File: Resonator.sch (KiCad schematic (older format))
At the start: 31 parts, among them U1 PCM3060

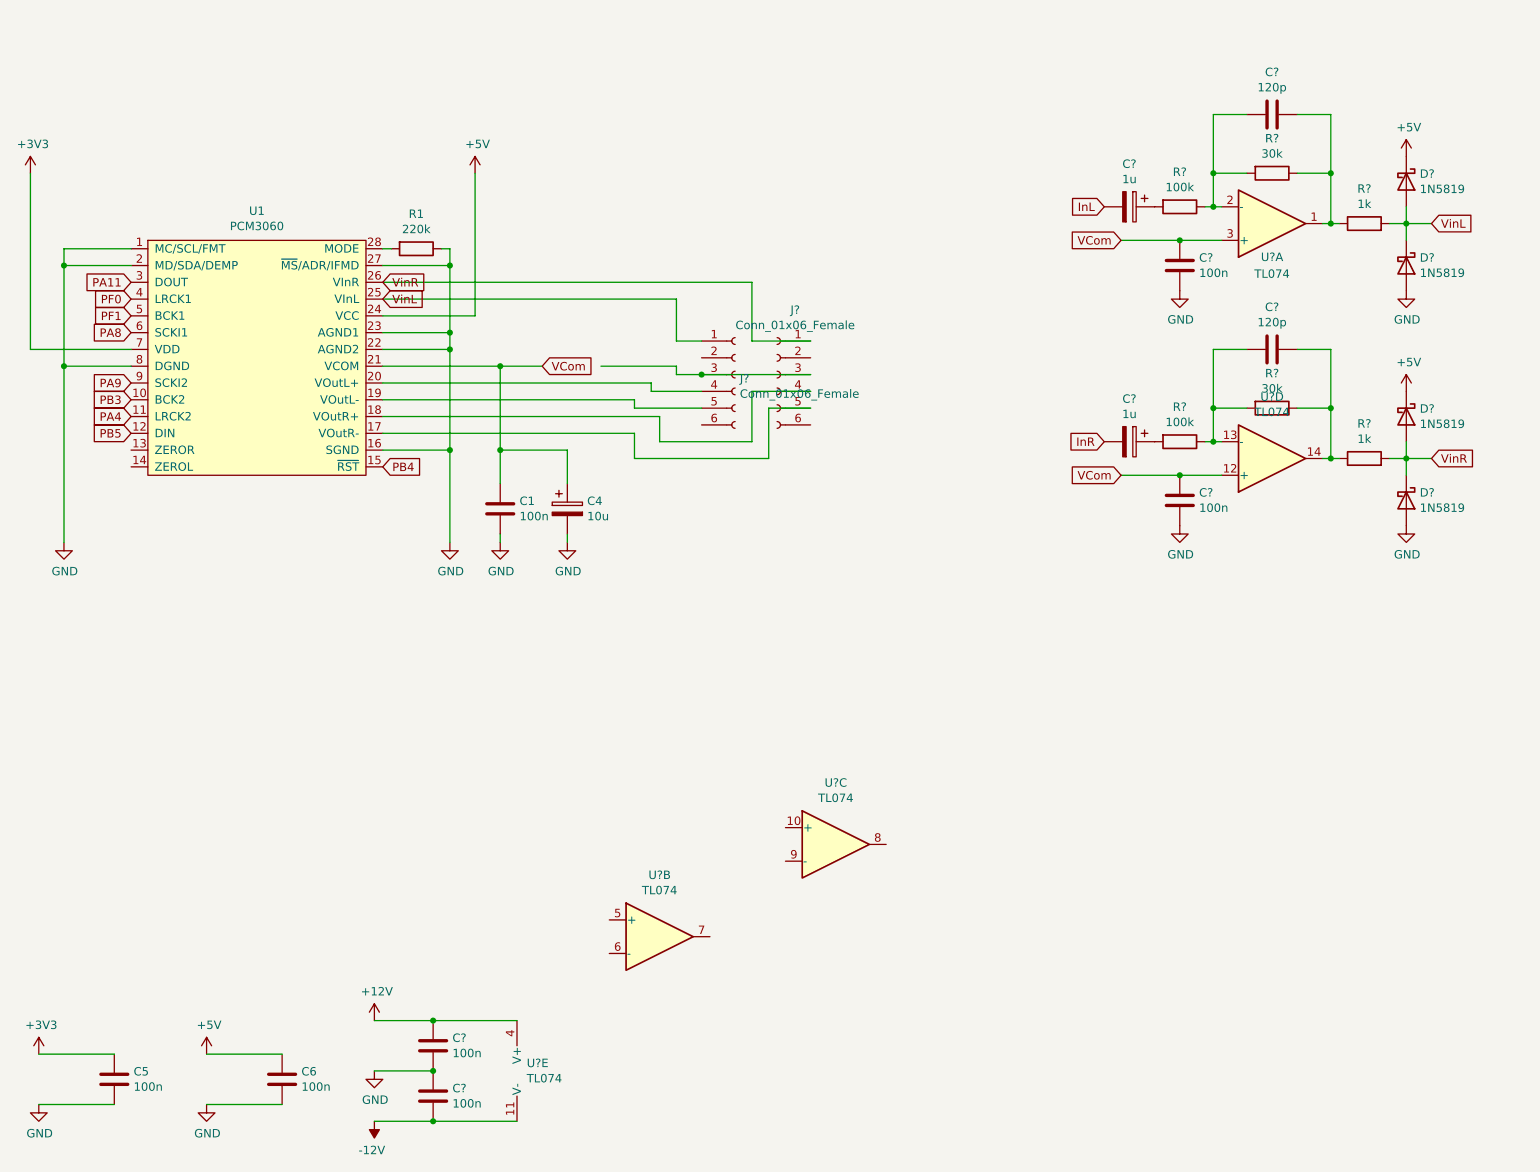
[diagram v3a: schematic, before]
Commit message: Output stage schematic.
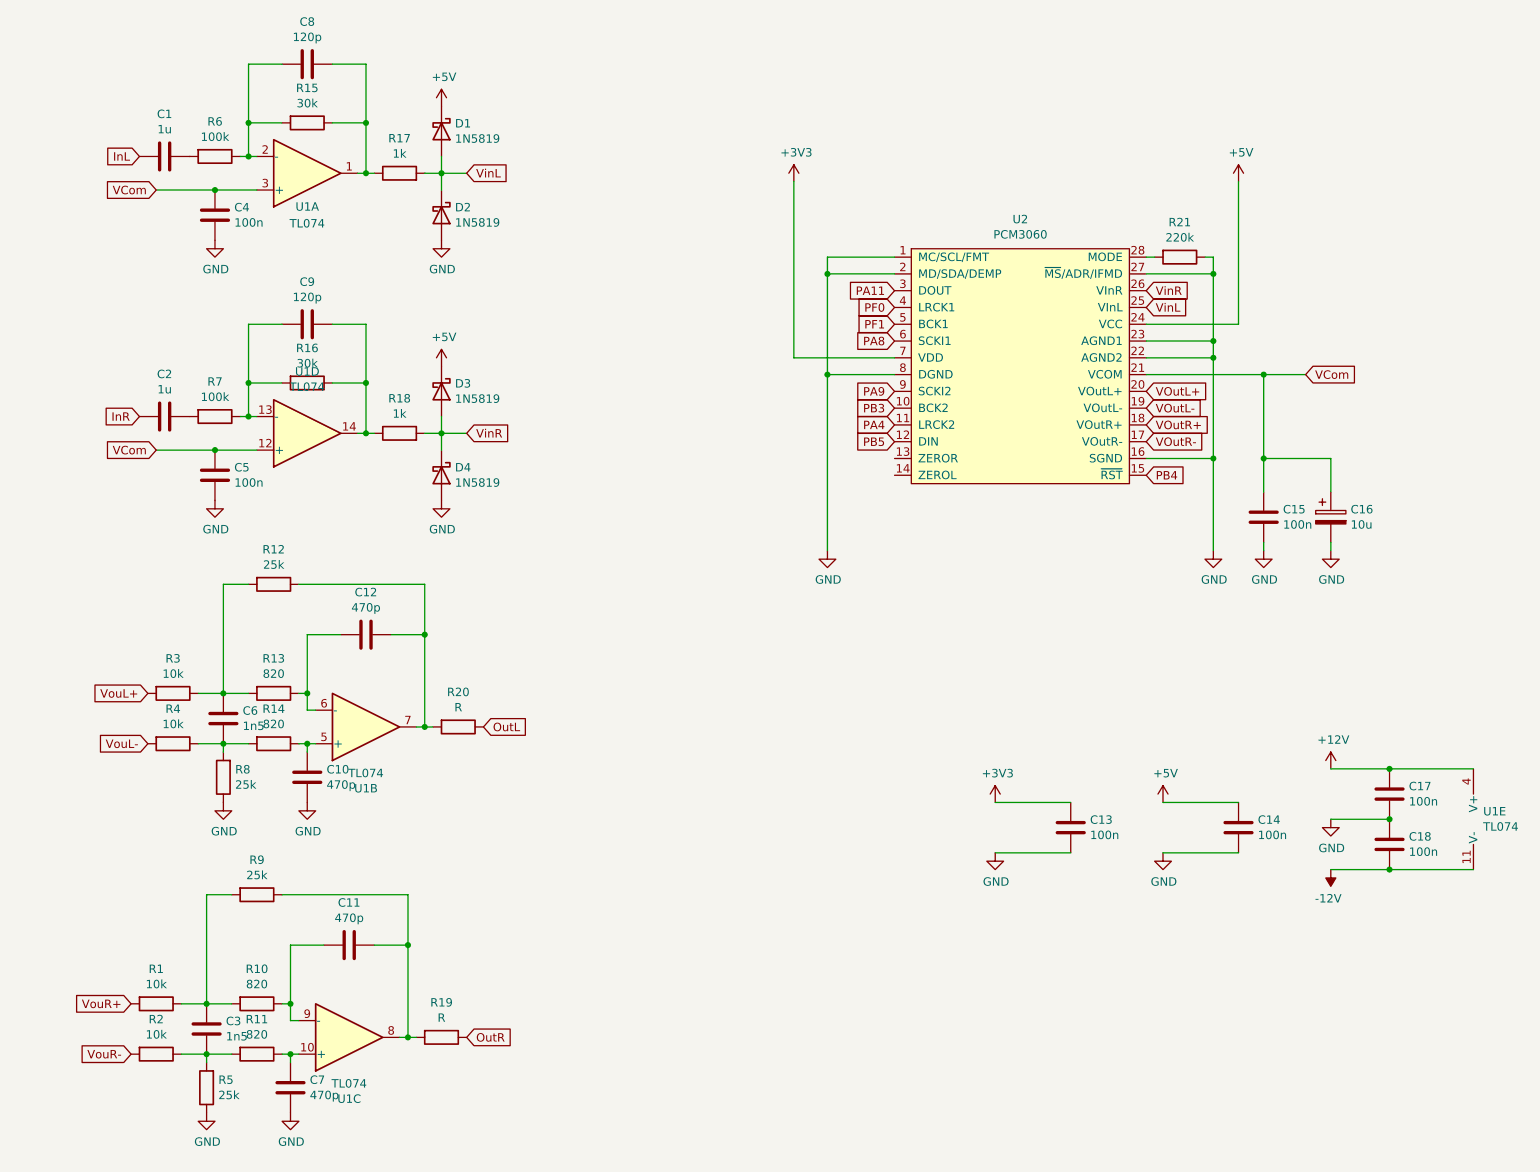
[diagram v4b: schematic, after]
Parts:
- removed C? (x2): 1u, symbol Device:CP
- removed J? (x2): Conn_01x06_Female, symbol Connector:Conn_01x06_Female
- added C1, C2: 1u, Capacitor_SMD:C_1210_3225Metric, symbol Device:C
- added C10, C11, C12, C7: 470p, symbol Device:C
- added C3, C6: 1n5, symbol Device:C
- added R1, R2, R3, R4: 10k, symbol Device:R
- added R10, R11, R13, R14: 820, symbol Device:R
- added R12, R5, R8, R9: 25k, symbol Device:R
- added R19, R20: R, symbol Device:R
- gave numbers to parts that had none: 17
- renumbered C5 to C13, C6 to C14, C1 to C15, C4 to C16, R1 to R21, U1 to U2
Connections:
- net GND: now also C10.2, C7.2, R5.1, R8.1
- net InL: now also C1.2
- net InR: now also C2.2
- net VOutR-: now reaches U2.17 (VOutR-)
- net VOutR+: now reaches U2.18 (VOutR+)
- net VOutL-: now reaches U2.19 (VOutL-)
- net VOutL+: now reaches U2.20 (VOutL+)
- net at U1.5 (+): now also C10.1, R14.1
- net at U1.6 (-): now also C12.2, R13.1
- net at U1.7: now also C12.1, R12.1, R20.2
- net at U1.10 (+): now also C7.1, R11.1
- net at U1.8: now also C11.1, R19.2, R9.1
- net at U1.9 (-): now also C11.2, R10.1
- net at R6.2: now also C1.1
- net at R7.2: now also C2.1
- new net: C3.1, R1.1, R10.2, R9.2
- new net: C3.2, R11.2, R2.1, R5.2
- new net: C6.1, R12.2, R13.2, R3.1
- new net: C6.2, R14.2, R4.1, R8.2
- new net OutL: R20.1
- new net OutR: R19.1
- new net VouL+: R3.2
- new net VouL-: R4.2
- new net VouR+: R1.2
- new net VouR-: R2.2
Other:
- moved on the sheet: C13, C14, C15, C16, C17, C18, C4, C5, C8, C9, D1, D2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

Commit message: Some early placement.
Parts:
- C10, C11, C12, C13, C14, C15, C16, C17, C18, C3, C4, C5, C6, C7, C8, C9: footprint (none) -> Capacitor_SMD:C_0603_1608Metric
- D1, D2, D3, D4: footprint (none) -> Diode_SMD:D_SOD-123
- R1, R10, R11, R12, R13, R14, R15, R16, R17, R18, R2, R21, R3, R4, R5, R6, R7, R8, R9: footprint (none) -> Resistor_SMD:R_0603_1608Metric
- R19, R20: value R -> 1k; footprint (none) -> Resistor_SMD:R_0603_1608Metric
- U1: footprint (none) -> Package_SO:TSSOP-14_4.4x5mm_P0.65mm
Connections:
- net VouL+ is gone; now on net VOutL+: R3.2
- net VouL- is gone; now on net VOutL-: R4.2
- net VouR+ is gone; now on net VOutR+: R1.2
- net VouR- is gone; now on net VOutR-: R2.2

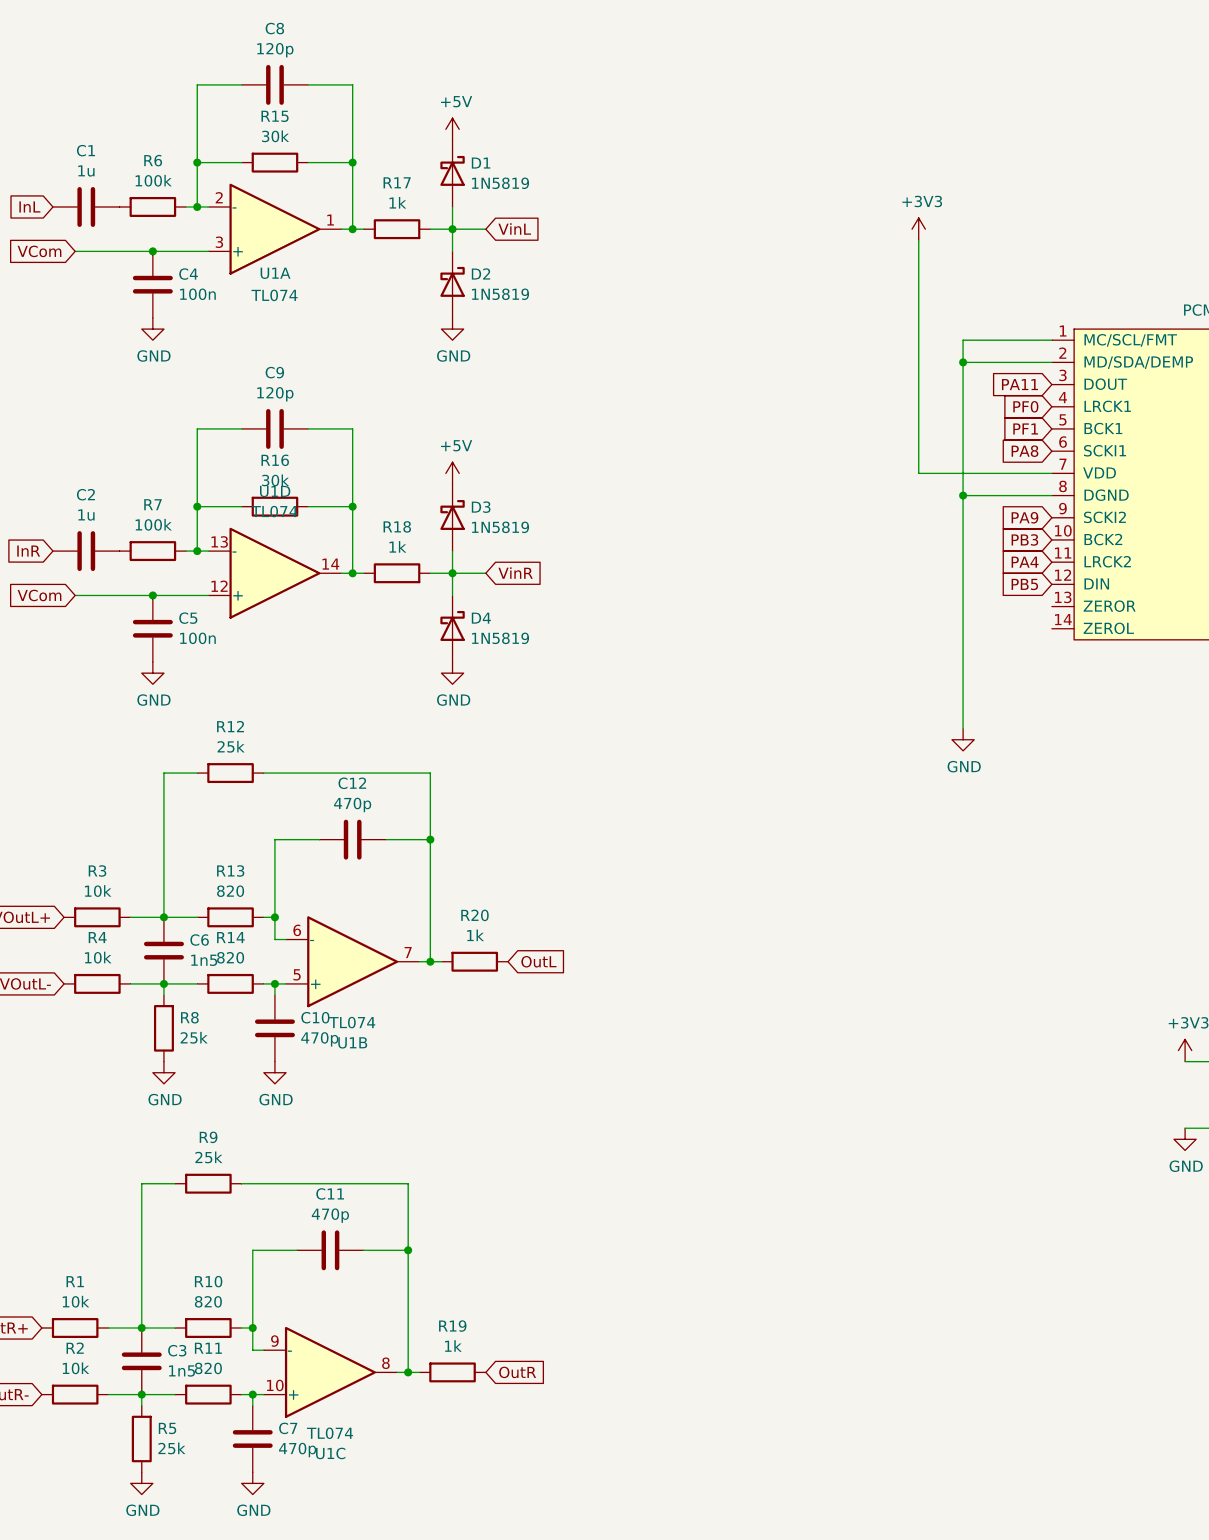
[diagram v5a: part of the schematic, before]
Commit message: Added power supply and adjusted gains for 12Vpp I/O.
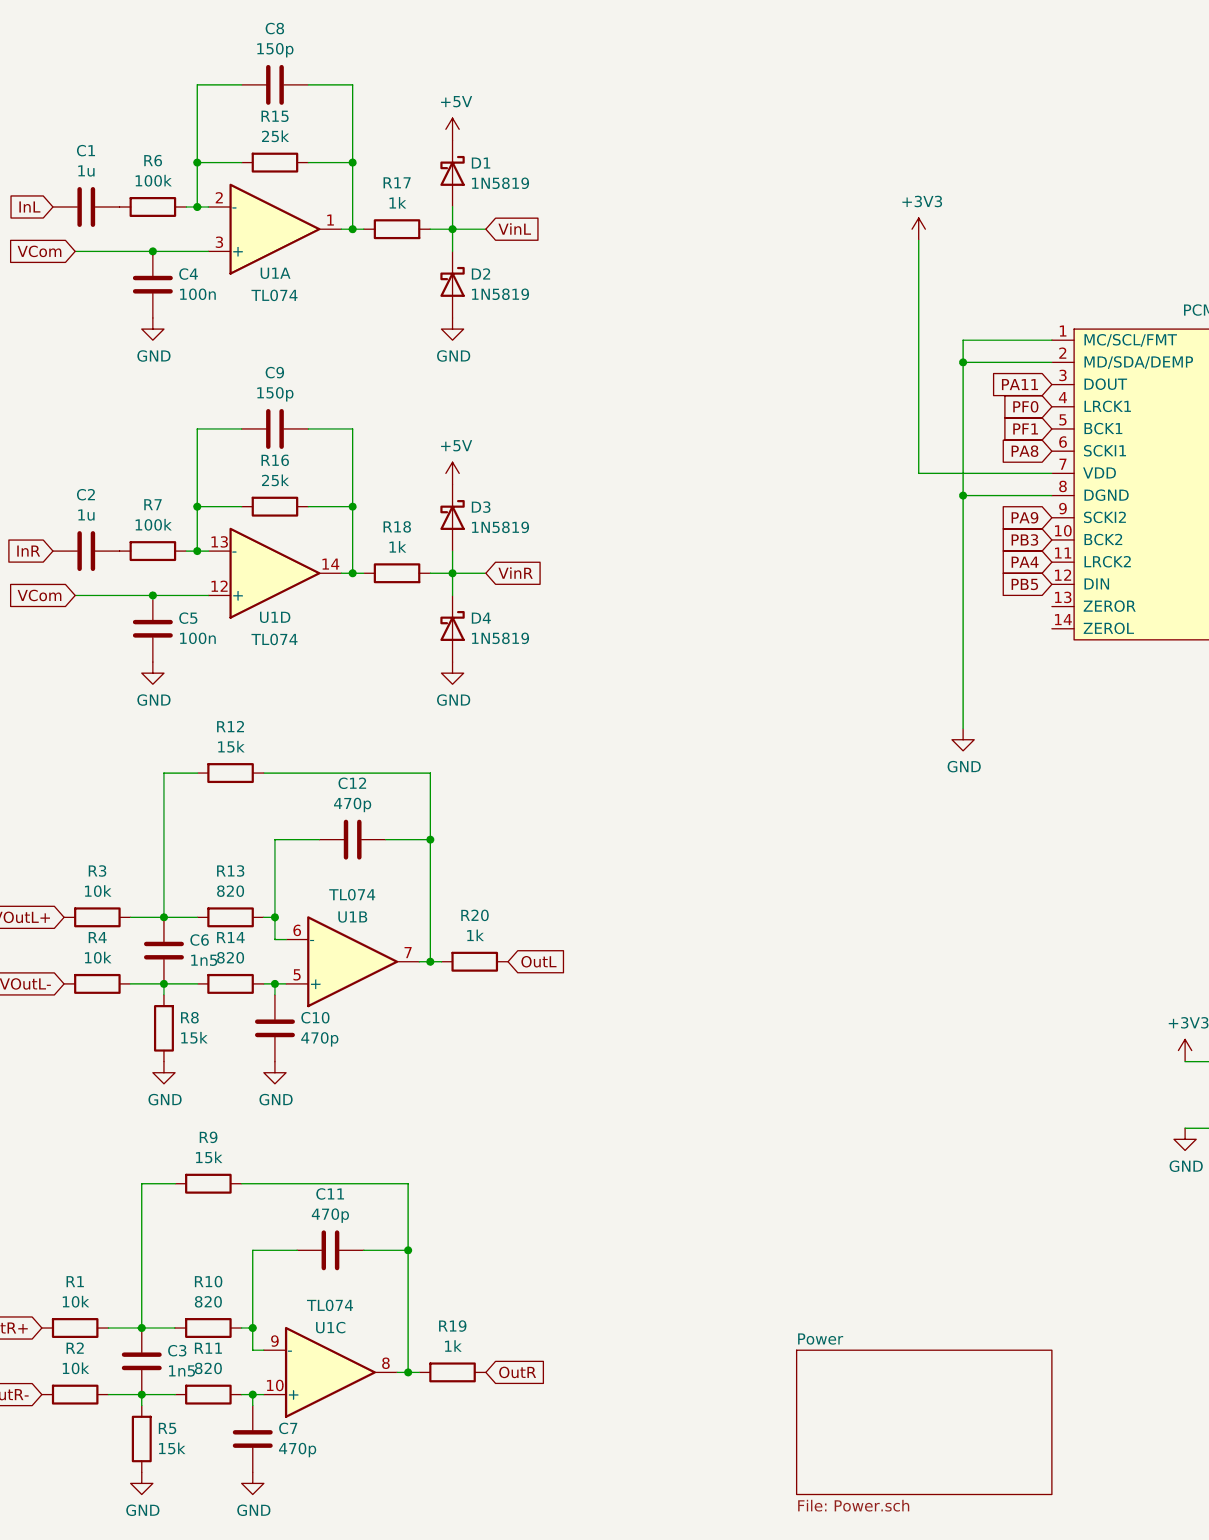
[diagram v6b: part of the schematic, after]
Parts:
- C8, C9: value 120p -> 150p
- R12, R5, R8, R9: value 25k -> 15k
- R15, R16: value 30k -> 25k
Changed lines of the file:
@@
 $Descr A4 11693 8268
 encoding utf-8
-Sheet 1 1
+Sheet 1 2
 Title "Resonator"
 Date "2021-11-21"
@@
 U 4 1 61A3FF95
 P 3150 3200
-F 0 "U1" H 3150 2833 50  0000 C CNN
-F 1 "TL074" H 3150 2924 50  0000 C CNN
+F 0 "U1" H 3150 3400 50  0000 C CNN
+F 1 "TL074" H 3150 3500 50  0000 C CNN
 F 2 "Package_SO:TSSOP-14_4.4x5mm_P0.65mm" H 3100 3300 50  0001 C CNN
 F 3 "http://www.ti.com/lit/ds/symlink/tl071.pdf" H 3200 3400 50  0001 C CNN
@@
 P 3150 1350
 F 0 "R15" V 2943 1350 50  0000 C CNN
-F 1 "30k" V 3034 1350 50  0000 C CNN
+F 1 "25k" V 3034 1350 50  0000 C CNN
 F 2 "Resistor_SMD:R_0603_1608Metric" V 3080 1350 50  0001 C CNN
 F 3 "~" H 3150 1350 50  0001 C CNN
@@
 P 3150 1000
 F 0 "C8" V 2898 1000 50  0000 C CNN
-F 1 "120p" V 2989 1000 50  0000 C CNN
+F 1 "150p" V 2989 1000 50  0000 C CNN
 F 2 "Capacitor_SMD:C_0603_1608Metric" H 3188 850 50  0001 C CNN
 F 3 "~" H 3150 1000 50  0001 C CNN
@@
 P 3150 2550
 F 0 "C9" V 2898 2550 50  0000 C CNN
-F 1 "120p" V 2989 2550 50  0000 C CNN
+F 1 "150p" V 2989 2550 50  0000 C CNN
 F 2 "Capacitor_SMD:C_0603_1608Metric" H 3188 2400 50  0001 C CNN
 F 3 "~" H 3150 2550 50  0001 C CNN
@@
 P 3150 2900
 F 0 "R16" V 2943 2900 50  0000 C CNN
-F 1 "30k" V 3034 2900 50  0000 C CNN
+F 1 "25k" V 3034 2900 50  0000 C CNN
 F 2 "Resistor_SMD:R_0603_1608Metric" V 3080 2900 50  0001 C CNN
 F 3 "~" H 3150 2900 50  0001 C CNN
@@
 U 2 1 61A340C7
 P 3500 4950
-F 0 "U1" H 3500 5317 50  0000 C CNN
-F 1 "TL074" H 3500 5226 50  0000 C CNN
+F 0 "U1" H 3500 4750 50  0000 C CNN
+F 1 "TL074" H 3500 4650 50  0000 C CNN
 F 2 "Package_SO:TSSOP-14_4.4x5mm_P0.65mm" H 3450 5050 50  0001 C CNN
 F 3 "http://www.ti.com/lit/ds/symlink/tl071.pdf" H 3550 5150 50  0001 C CNN
@@
 U 3 1 61A3E11D
 P 3400 6800
-F 0 "U1" H 3400 7167 50  0000 C CNN
-F 1 "TL074" H 3400 7076 50  0000 C CNN
+F 0 "U1" H 3400 6600 50  0000 C CNN
+F 1 "TL074" H 3400 6500 50  0000 C CNN
 F 2 "Package_SO:TSSOP-14_4.4x5mm_P0.65mm" H 3350 6900 50  0001 C CNN
 F 3 "http://www.ti.com/lit/ds/symlink/tl071.pdf" H 3450 7000 50  0001 C CNN
@@
 P 2850 5950
 F 0 "R9" V 2643 5950 50  0000 C CNN
-F 1 "25k" V 2734 5950 50  0000 C CNN
+F 1 "15k" V 2734 5950 50  0000 C CNN
 F 2 "Resistor_SMD:R_0603_1608Metric" V 2780 5950 50  0001 C CNN
 F 3 "~" H 2850 5950 50  0001 C CNN
@@
 P 2550 7100
 F 0 "R5" H 2480 7054 50  0000 R CNN
-F 1 "25k" H 2480 7145 50  0000 R CNN
+F 1 "15k" H 2480 7145 50  0000 R CNN
 F 2 "Resistor_SMD:R_0603_1608Metric" V 2480 7100 50  0001 C CNN
 F 3 "~" H 2550 7100 50  0001 C CNN
@@
 P 2950 4100
 F 0 "R12" V 2743 4100 50  0000 C CNN
-F 1 "25k" V 2834 4100 50  0000 C CNN
+F 1 "15k" V 2834 4100 50  0000 C CNN
 F 2 "Resistor_SMD:R_0603_1608Metric" V 2880 4100 50  0001 C CNN
 F 3 "~" H 2950 4100 50  0001 C CNN
@@
 P 2650 5250
 F 0 "R8" H 2580 5204 50  0000 R CNN
-F 1 "25k" H 2580 5295 50  0000 R CNN
+F 1 "15k" H 2580 5295 50  0000 R CNN
 F 2 "Resistor_SMD:R_0603_1608Metric" V 2580 5250 50  0001 C CNN
 F 3 "~" H 2650 5250 50  0001 C CNN
@@
 	1    0    0    -1
 $EndComp
+$Sheet
+S 5500 6700 1150 650
+U 61C80AC7
+F0 "Power" 50
+F1 "Power.sch" 50
+$EndSheet
 $EndSCHEMATC

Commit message: Moved audio-io to separate sheet.
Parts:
- removed C1, C2: 1u, Capacitor_SMD:C_1210_3225Metric, symbol Device:C
- removed C10, C11, C12, C7: 470p, Capacitor_SMD:C_0603_1608Metric, symbol Device:C
- removed C17, C18, C4, C5: 100n, Capacitor_SMD:C_0603_1608Metric, symbol Device:C
- removed C3, C6: 1n5, Capacitor_SMD:C_0603_1608Metric, symbol Device:C
- removed C8, C9: 150p, Capacitor_SMD:C_0603_1608Metric, symbol Device:C
- removed D1, D2, D3, D4: 1N5819, Diode_SMD:D_SOD-123, symbol Device:D_Schottky
- removed R1, R2, R3, R4: 10k, Resistor_SMD:R_0603_1608Metric, symbol Device:R
- removed R10, R11, R13, R14: 820, Resistor_SMD:R_0603_1608Metric, symbol Device:R
- removed R12, R5, R8, R9: 15k, Resistor_SMD:R_0603_1608Metric, symbol Device:R
- removed R15, R16: 25k, Resistor_SMD:R_0603_1608Metric, symbol Device:R
- removed R17, R18, R19, R20: 1k, Resistor_SMD:R_0603_1608Metric, symbol Device:R
- removed R6, R7: 100k, Resistor_SMD:R_0603_1608Metric, symbol Device:R
- removed U1: TL074, Package_SO:TSSOP-14_4.4x5mm_P0.65mm, symbol Amplifier_Operational:TL074
- renumbered C13 to C1, C14 to C2, C15 to C3, C16 to C4, R21 to R1, U2 to U1
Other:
- moved on the sheet: C1, C2, C3, C4, R1, U1
